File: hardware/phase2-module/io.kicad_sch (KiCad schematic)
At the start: 6 parts, among them J1 SLOT PWR BLADES, J4 OUTPUT 30A, J5 SLOT SIGNALS, J6 FAN, Q8 2N7002

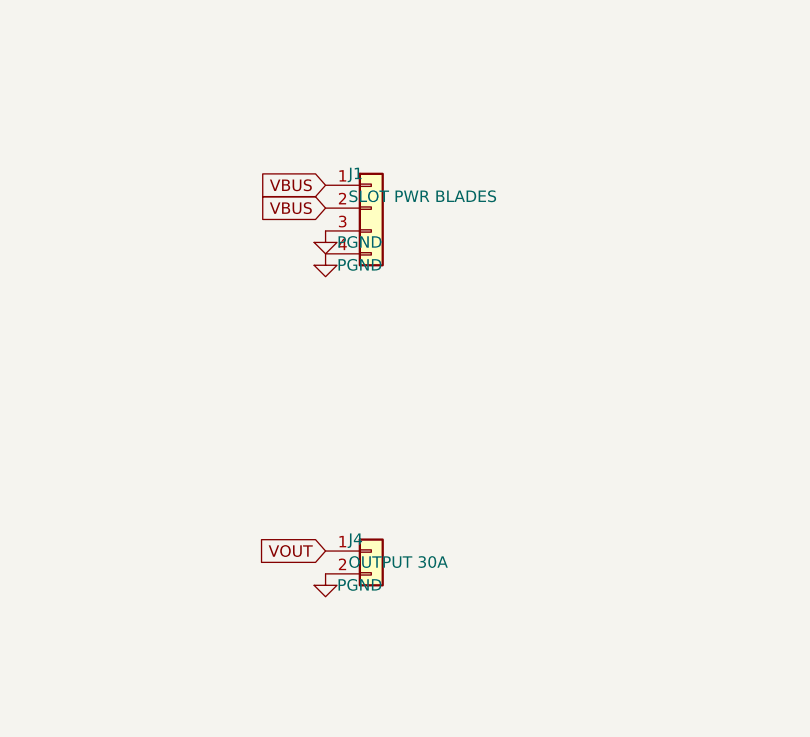
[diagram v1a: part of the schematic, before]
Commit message: Apply China-sourcing engineering changes across all boards + mechanical frame
All datasheet-verified before application (details hardware/SOURCING.md sF):
- TMUX1101 -> TS5A3166DBVR (LCSC availability; ts5a3166.pdf: pin POSITIONS
  identical - 1=NO 2=COM 3=GND 4=IN 5=V+; VIH 2.4V ok from 3.3V GPIO)
- TLV7011 DBVR -> DCKR: tlv7022.pdf shows DBV/DCK share one pinout, so
  footprint-only (SOT-353_SC-70-5); SOT-23-5 stock in China is nearly gone
- crystal load caps 10p -> 18p, both phases (CL=12pF China crystals; the
  HANDOVER-blessed alternative to hunting CL=8pF parts)
- Phase-1 inductor -> MWSA1707S-100MT (JLCPCB-verified 16.5A Isat/10.5A
  Irms vs 12A/8A required); value strings now dual-source Sunlord/Coilcraft
- module slot power + P2 output -> XT60PW-M (2-pin), backplane slots ->
  XT60PW-F; bus shunt -> 2x BVS-M-R0005 parallel (the exact-net checker
  caught RS1/RS2 placed one pin-span apart merging VBUS_IN into VBUS)
- 470u bulk -> THT radial D10; output MLCCs 22u -> 10u/50V X7S; buzzer ->
  MLT-8530 (fp placeholder)
All four checker chains green: 137/173/30/80 components.

hardware/MECHANICAL.md (frozen): 30mm slot pitch, P2 130x90 4-layer,
backplane ~330x100 2-layer 2oz, manager 100x80; cost-first stackup (1oz
outer + solder-reinforced bus, 2oz only if the thermal soak demands it);
inductor footprint = SUPERSET pattern accepting Sunlord 1707 AND Coilcraft
XAL1510 so the A/B pair is a pure part swap.

HANDOVER: sub-0.5V mV-accurate output DEFERRED to a future dedicated
linear post-regulator module (user decision 2026-07-18); buck floors
documented (P2 0.7V @30V bus, P1 0.5V).

Co-Authored-By: Claude Fable 5 <noreply@anthropic.com>
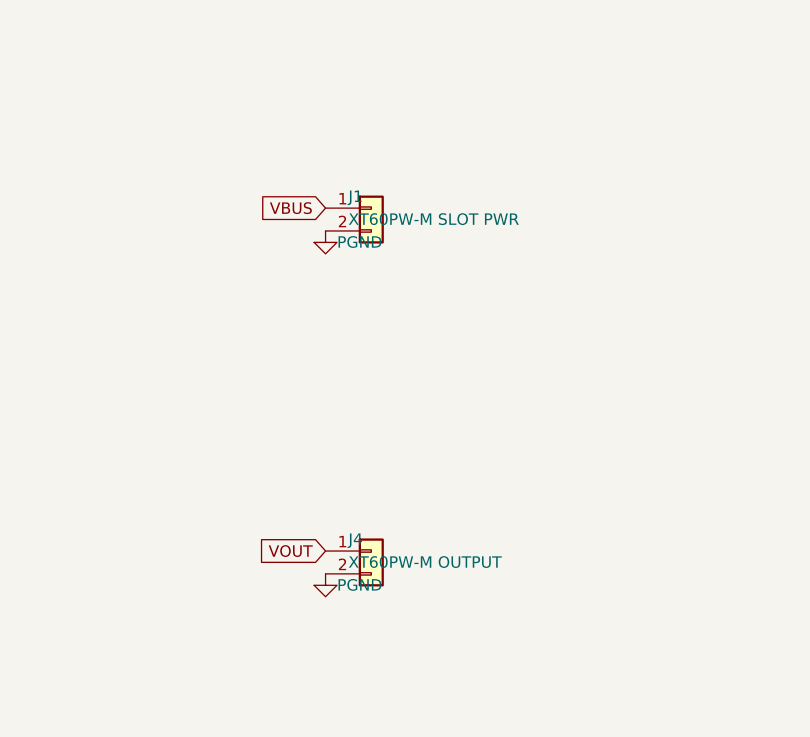
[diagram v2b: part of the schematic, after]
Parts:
- removed J1: SLOT PWR BLADES, Connector_PinHeader_2.54mm:PinHeader_1x04_P2.54mm_Vertical, symbol Connector_Generic:Conn_01x04
- added J1: XT60PW-M SLOT PWR, Connector_PinHeader_2.54mm:PinHeader_1x02_P2.54mm_Vertical, symbol Connector_Generic:Conn_01x02
- J4: value OUTPUT 30A -> XT60PW-M OUTPUT; footprint TerminalBlock_Phoenix:TerminalBlock_Phoenix_PT-1,5-2-5.0-H_1x02_P5.00mm_Horizontal -> Connector_PinHeader_2.54mm:PinHeader_1x02_P2.54mm_Vertical
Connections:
- net PGND: now also J1.2 (Pin_2)
- net VBUS: now also J1.1 (Pin_1)

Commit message: Footprint pass: China-part land patterns generated, placeholders retired
build_fplib.py sourcing_footprints() - geometry vetted from LCSC/EasyEDA
library pulls (easyeda2kicad), encoded in code like the PowerFET precedent
so regeneration needs no network:
- XT60PW-M / XT60PW-F: power pins 3.8mm pads / 2.9-2.8mm drills @ 7.2mm
  pitch + 0.6x1.6 retention slots. The -F library pull had the RETENTION
  LEGS numbered as pads 1,2 - power pads renumbered to 1,2 to match the -M
  and the Conn_01x02 symbol (a trap no netlist check would ever catch)
- L_1707_XAL1510: SUPERSET pad 5.39x13.2 @ +/-6.405 covering Sunlord
  MWSA1707S (3.5x12.8 @ 7.35) and Coilcraft XAL1510 (3.18x13.2 @ 5.3) -
  the A/B thermal pair and the P1 10uH are pure part swaps
- R3920_BVS bar shunt, MLT-8530 buzzer (edge pads paired 1,1/2,2)
Generators swapped off placeholders (P1 L1, P2 L1/L3/J1/J4, backplane
slots+RS pair, manager buzzer); all four chains green (137/173/30/80).

MECHANICAL.md: insertion geometry corrected to server-PSU style (vertical
rear backplane, modules slide horizontally; XT60 height stagger = power-
first mating). HARD GATE added: XT60 +/- pad mating is ASSUMED until a
mated pair is buzzed out on arrival - required before gerber submission.

Co-Authored-By: Claude Fable 5 <noreply@anthropic.com>
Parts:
- J1, J4: footprint Connector_PinHeader_2.54mm:PinHeader_1x02_P2.54mm_Vertical -> labbench:XT60PW-M
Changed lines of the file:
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@@
     (property "Reference" "J1" (at 35.56 77.47 0) (effects (font (size 1.27 1.27)) (justify left)))
     (property "Value" "XT60PW-M SLOT PWR" (at 35.56 80.00999999999999 0) (effects (font (size 1.27 1.27)) (justify left)))
-    (property "Footprint" "Connector_PinHeader_2.54mm:PinHeader_1x02_P2.54mm_Vertical" (at 38.1 78.74 0) (effects (font (size 1.27 1.27)) hide))
+    (property "Footprint" "labbench:XT60PW-M" (at 38.1 78.74 0) (effects (font (size 1.27 1.27)) hide))
     (property "Datasheet" "~" (at 38.1 78.74 0) (effects (font (size 1.27 1.27)) hide))
     (pin "1")
@@
     (property "Reference" "J4" (at 35.56 115.57000000000001 0) (effects (font (size 1.27 1.27)) (justify left)))
     (property "Value" "XT60PW-M OUTPUT" (at 35.56 118.11 0) (effects (font (size 1.27 1.27)) (justify left)))
-    (property "Footprint" "Connector_PinHeader_2.54mm:PinHeader_1x02_P2.54mm_Vertical" (at 38.1 116.84 0) (effects (font (size 1.27 1.27)) hide))
+    (property "Footprint" "labbench:XT60PW-M" (at 38.1 116.84 0) (effects (font (size 1.27 1.27)) hide))
     (property "Datasheet" "~" (at 38.1 116.84 0) (effects (font (size 1.27 1.27)) hide))
     (pin "1")
